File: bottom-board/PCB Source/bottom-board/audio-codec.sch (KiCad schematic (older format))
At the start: 27 parts, among them U13 AP2120N-3.3, U3 CS4265

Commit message: rev 0.0.3
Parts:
- removed C14: 10uF, Capacitor_SMD:C_0603_1608Metric, symbol bottom-board-rescue:C_Small
- removed C22: 100nF, Capacitor_SMD:C_0603_1608Metric, symbol bottom-board-rescue:C_Small
- removed FB2, FB3: Ferrite_Bead, Resistor_SMD:R_0603_1608Metric, symbol Device:Ferrite_Bead
- added C73, C75, C77, C79, C81, C94: 100nF, Capacitor_SMD:C_0603_1608Metric, symbol bottom-board-rescue:C_Small
- added C76, C78, C80: 10uF, Capacitor_SMD:C_0805_2012Metric, symbol bottom-board-rescue:C_Small
- added X1: 24.576MHz, Oscillator:Oscillator_SMD_Abracon_ASV-4Pin_7.0x5.1mm, symbol Oscillator:ASCO
- C24: footprint Capacitor_SMD:C_0805_2012Metric -> Capacitor_SMD:C_0603_1608Metric; MPN C2012X7R1E105K125AB -> FCA1210C105M-G2
- D10, D11: symbol Diode:BAT54S -> bottom-board-rescue:BAT54S-Diode
- FB1: symbol Device:Ferrite_Bead -> bottom-board-rescue:Ferrite_Bead-Device
- R1, R11, R2: value 10k -> 2K7; MPN RMCF0603JT10K0 -> CRGCQ0603F2K7
- R10, R9: MPN RMCF0603JT100R -> RMCF0603JT22R0
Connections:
- wire segments 128 -> 155
- no-connect marks 3 -> 6
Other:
- note added: "Codec MCLK"
- note added: "The series resistor at I2S_MCLK \nmust only be placed when the xtal\nis not placed, and vice versa."
- note added: "VA"
- note added: "VD"
- note added: "VLC"
- note added: "VLS"
- moved on the sheet: R3

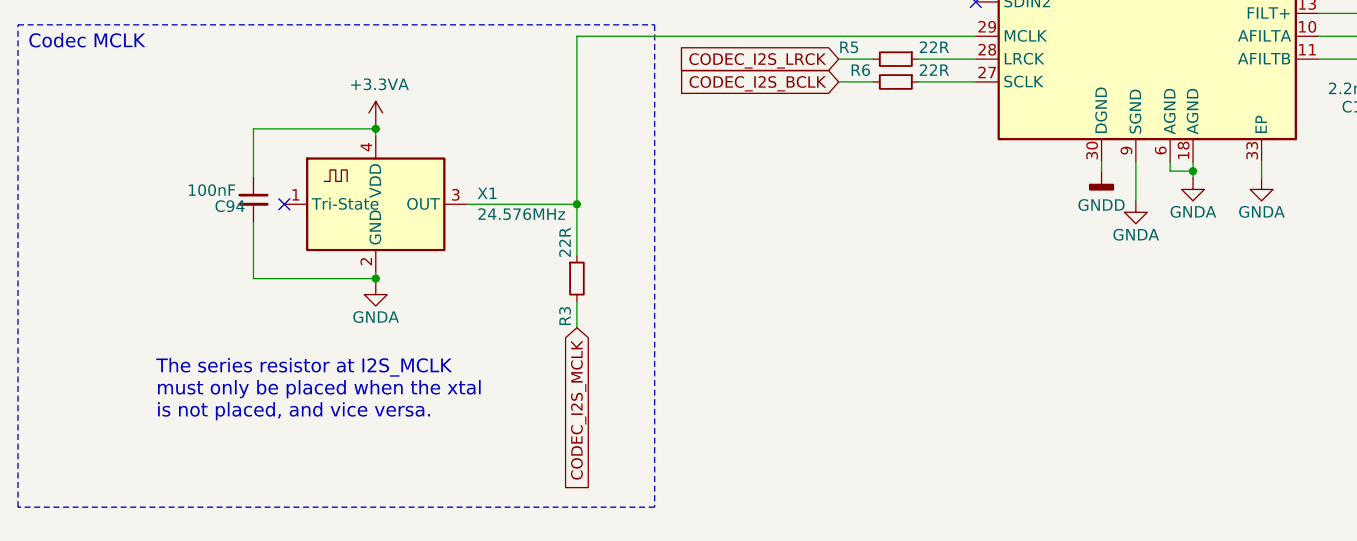
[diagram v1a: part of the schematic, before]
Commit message: change design to 4 layer PCB
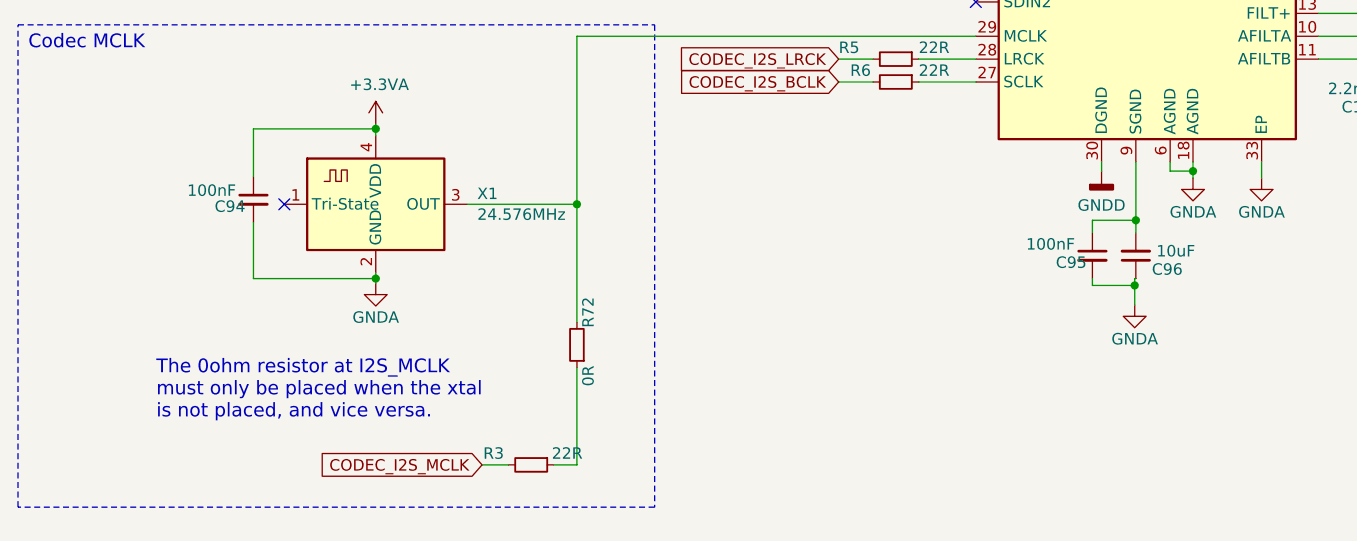
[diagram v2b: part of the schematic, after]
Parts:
- added C95: 100nF, Capacitor_SMD:C_0603_1608Metric, symbol bottom-board-rescue:C_Small
- added C96: 10uF, Capacitor_SMD:C_0603_1608Metric, symbol bottom-board-rescue:C_Small
- added R72: 0R, Resistor_SMD:R_0603_1608Metric, symbol bottom-board-rescue:R_Small
- C24: MPN FCA1210C105M-G2 -> TMK107B7105KA-T
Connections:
- net GNDA: now also C95.2, C96.1; no longer U3.9 (SGND)
- net at U3.29 (MCLK), X1.3 (OUT): now also R72.2; no longer R3.1
- new net: R3.1, R72.1
- new net: C95.1, C96.2, U3.9 (SGND)
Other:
- note added: "The 0ohm resistor at I2S_MCLK \nmust only be placed when the xtal\nis not placed, and vice versa."
- note removed: "The series resistor at I2S_MCLK \nmust only be placed when the xtal\nis not placed, and vice versa."
- moved on the sheet: R3
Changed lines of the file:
@@
 F 2 "Capacitor_SMD:C_0603_1608Metric" H 1500 1600 60  0001 C CNN
 F 3 "" H 1500 1600 60  0000 C CNN
-F 4 "FCA1210C105M-G2" H -2950 -100 50  0001 C CNN "MPN"
+F 4 "TMK107B7105KA-T" H -2950 -100 50  0001 C CNN "MPN"
 	1    1500 1600
 	-1   0    0    1
@@
 Text GLabel 4470 4040 0    50   Input ~ 0
 CODEC_I2S_LRCK
-Text GLabel 3325 5215 3    50   Input ~ 0
+Text GLabel 2910 5815 0    50   Input ~ 0
 CODEC_I2S_MCLK
 Wire Wire Line
@@
 L bottom-board-rescue:R_Small R3
 U 1 1 5C7E5062
-P 3325 5000
-F 0 "R3" V 3275 4790 50  0000 L CNN
-F 1 "22R" V 3275 5090 50  0000 L CNN
-F 2 "Resistor_SMD:R_0603_1608Metric" H 3325 5000 60  0001 C CNN
-F 3 "" H 3325 5000 60  0000 C CNN
-F 4 "RMCF0603JT22R0" H -975 2650 50  0001 C CNN "MPN"
-	1    3325 5000
-	1    0    0    -1
+P 3125 5815
+F 0 "R3" V 3075 5605 50  0000 L CNN
+F 1 "22R" V 3075 5905 50  0000 L CNN
+F 2 "Resistor_SMD:R_0603_1608Metric" H 3125 5815 60  0001 C CNN
+F 3 "" H 3125 5815 60  0000 C CNN
+F 4 "RMCF0603JT22R0" H -1175 3465 50  0001 C CNN "MPN"
+	1    3125 5815
+	0    1    1    0
 $EndComp
 Wire Wire Line
@@
 NoConn ~ 6570 3090
 NoConn ~ 5070 3790
-Wire Wire Line
-	5770 4490 5770 4660
 $Comp
 L bottom-board-rescue:GNDA-power #PWR?
 U 1 1 5F120097
-P 5770 4660
+P 5765 5115
 AR Path="/5F120097" Ref="#PWR?"  Part="1"
 AR Path="/54F72B97/5F120097" Ref="#PWR0130"  Part="1"
-F 0 "#PWR0130" H 5770 4410 50  0001 C CNN
-F 1 "GNDA" H 5770 4510 50  0000 C CNN
-F 2 "" H 5770 4660 60  0000 C CNN
-F 3 "" H 5770 4660 60  0000 C CNN
-	1    5770 4660
+F 0 "#PWR0130" H 5765 4865 50  0001 C CNN
+F 1 "GNDA" H 5765 4965 50  0000 C CNN
+F 2 "" H 5765 5115 60  0000 C CNN
+F 3 "" H 5765 5115 60  0000 C CNN
+	1    5765 5115
 	1    0    0    -1
 $EndComp
@@
 NoConn ~ 5070 2940
 Wire Wire Line
-	3325 5215 3325 5100
+	2910 5815 3025 5815
 $Comp
 L Oscillator:ASCO X1
@@
 $EndComp
 Text Notes 1485 5620 0    60   ~ 0
-The series resistor at I2S_MCLK \nmust only be placed when the xtal\nis not placed, and vice versa.
+The 0ohm resistor at I2S_MCLK \nmust only be placed when the xtal\nis not placed, and vice versa.
 Wire Wire Line
 	2445 4375 2445 4345
@@
 	2445 5000 2445 5020
 Connection ~ 2445 5000
-Wire Wire Line
-	3325 4900 3325 4675
 Wire Wire Line
 	3325 3940 5070 3940
@@
 Text Notes 925  4005 0    60   ~ 0
 Codec MCLK
+$Comp
+L bottom-board-rescue:C_Small C95
+U 1 1 5FB9A0FE
+P 5580 4900
+F 0 "C95" H 5420 4870 50  0000 L CNN
+F 1 "100nF" H 5290 4950 50  0000 L CNN
+F 2 "Capacitor_SMD:C_0603_1608Metric" H 5580 4900 60  0001 C CNN
+F 3 "" H 5580 4900 60  0000 C CNN
+F 4 "GCM188R71C104KA37D" H 280 -450 50  0001 C CNN "MPN"
+	1    5580 4900
+	1    0    0    -1
+$EndComp
+$Comp
+L bottom-board-rescue:C_Small C96
+U 1 1 5FB9A105
+P 5770 4900
+F 0 "C96" H 5700 4960 50  0000 R CNN
+F 1 "10uF" H 5510 4880 50  0000 L CNN
+F 2 "Capacitor_SMD:C_0603_1608Metric" H 5770 4900 60  0001 C CNN
+F 3 "" H 5770 4900 60  0000 C CNN
+F 4 "CL10A106MQ8NNNC" H 1320 3200 50  0001 C CNN "MPN"
+	1    5770 4900
+	-1   0    0    1
+$EndComp
+Wire Wire Line
+	5770 4490 5770 4745
+Wire Wire Line
+	5765 5115 5765 5030
+Wire Wire Line
+	5765 5000 5770 5000
+Wire Wire Line
+	5580 5000 5580 5030
+Wire Wire Line
+	5580 5030 5765 5030
+Connection ~ 5765 5030
+Wire Wire Line
+	5765 5030 5765 5000
+Wire Wire Line
+	5580 4800 5580 4745
+Wire Wire Line
+	5580 4745 5770 4745
+Connection ~ 5770 4745
+Wire Wire Line
+	5770 4745 5770 4800
+$Comp
+L bottom-board-rescue:R_Small R72
+U 1 1 5FC83DD5
+P 3325 5290
+F 0 "R72" V 3275 5080 50  0000 L CNN
+F 1 "0R" V 3275 5380 50  0000 L CNN
+F 2 "Resistor_SMD:R_0603_1608Metric" H 3325 5290 60  0001 C CNN
+F 3 "" H 3325 5290 60  0000 C CNN
+F 4 "" H -975 2940 50  0001 C CNN "MPN"
+	1    3325 5290
+	-1   0    0    1
+$EndComp
+Wire Wire Line
+	3225 5815 3325 5815
+Wire Wire Line
+	3325 5815 3325 5390
+Wire Wire Line
+	3325 4675 3325 5190
 $EndSCHEMATC

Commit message: cleanup BOM lines
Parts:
- C20, C96: MPN CL10A106MQ8NNNC -> EMK107BBJ106MA-T
- R72: MPN (none) -> RMCF0603ZT0R00
- X1: MPN ASV-24.576MHZ-EJ-T -> DO NOT PLACE
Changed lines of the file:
@@
 encoding utf-8
 Sheet 3 11
-Title "MOD Uno - Main Board"
-Date "2019-08-16"
-Rev "0.1"
+Title "MOD Dwarf - Main Board"
+Date "2021-04-07"
+Rev "1.2"
 Comp "MOD Devices GmbH"
-Comment1 "Uno Audio processing board"
-Comment2 "https://github.com/moddevices/hw-mod-uno"
+Comment1 "Dwarf Audio processing board"
+Comment2 "https://github.com/moddevices/hw-mod-dwarf"
 Comment3 "Inp Power: 12V 500mA"
 Comment4 "USB outp Power: 500mA"
@@
 F 2 "Capacitor_SMD:C_0603_1608Metric" H 7870 4150 60  0001 C CNN
 F 3 "" H 7870 4150 60  0000 C CNN
-F 4 "CL10A106MQ8NNNC" H 3420 2450 50  0001 C CNN "MPN"
+F 4 "EMK107BBJ106MA-T" H 3420 2450 50  0001 C CNN "MPN"
 	1    7870 4150
 	-1   0    0    1
@@
 F 2 "Oscillator:Oscillator_SMD_Abracon_ASV-4Pin_7.0x5.1mm" H 2545 4325 50  0001 C CNN
 F 3 "" H 2220 4800 50  0001 C CNN
-F 4 "ASV-24.576MHZ-EJ-T" H 2445 4675 50  0001 C CNN "MPN"
+F 4 "DO NOT PLACE" H 2445 4675 50  0001 C CNN "MPN"
 	1    2445 4675
 	1    0    0    -1
@@
 F 2 "Capacitor_SMD:C_0603_1608Metric" H 5770 4900 60  0001 C CNN
 F 3 "" H 5770 4900 60  0000 C CNN
-F 4 "CL10A106MQ8NNNC" H 1320 3200 50  0001 C CNN "MPN"
+F 4 "EMK107BBJ106MA-T" H 1320 3200 50  0001 C CNN "MPN"
 	1    5770 4900
 	-1   0    0    1
@@
 F 2 "Resistor_SMD:R_0603_1608Metric" H 3325 5290 60  0001 C CNN
 F 3 "" H 3325 5290 60  0000 C CNN
-F 4 "" H -975 2940 50  0001 C CNN "MPN"
+F 4 "RMCF0603ZT0R00" H -975 2940 50  0001 C CNN "MPN"
 	1    3325 5290
 	-1   0    0    1
